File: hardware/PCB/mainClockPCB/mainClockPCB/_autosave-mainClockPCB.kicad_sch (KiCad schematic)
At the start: 51 parts, among them IC2 SPX1117M3-L_TR, IC3 MCP7940N-I_P, IC4 PAM8904QJER, J1 USB_C_Receptacle_USB2.0_16P, J2 Conn_01x09_Socket, J3 Conn_01x02_Socket, J4 Conn_01x09_Socket, J5 Conn_01x06, SW1 SW_Push, SW2 SW_Push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

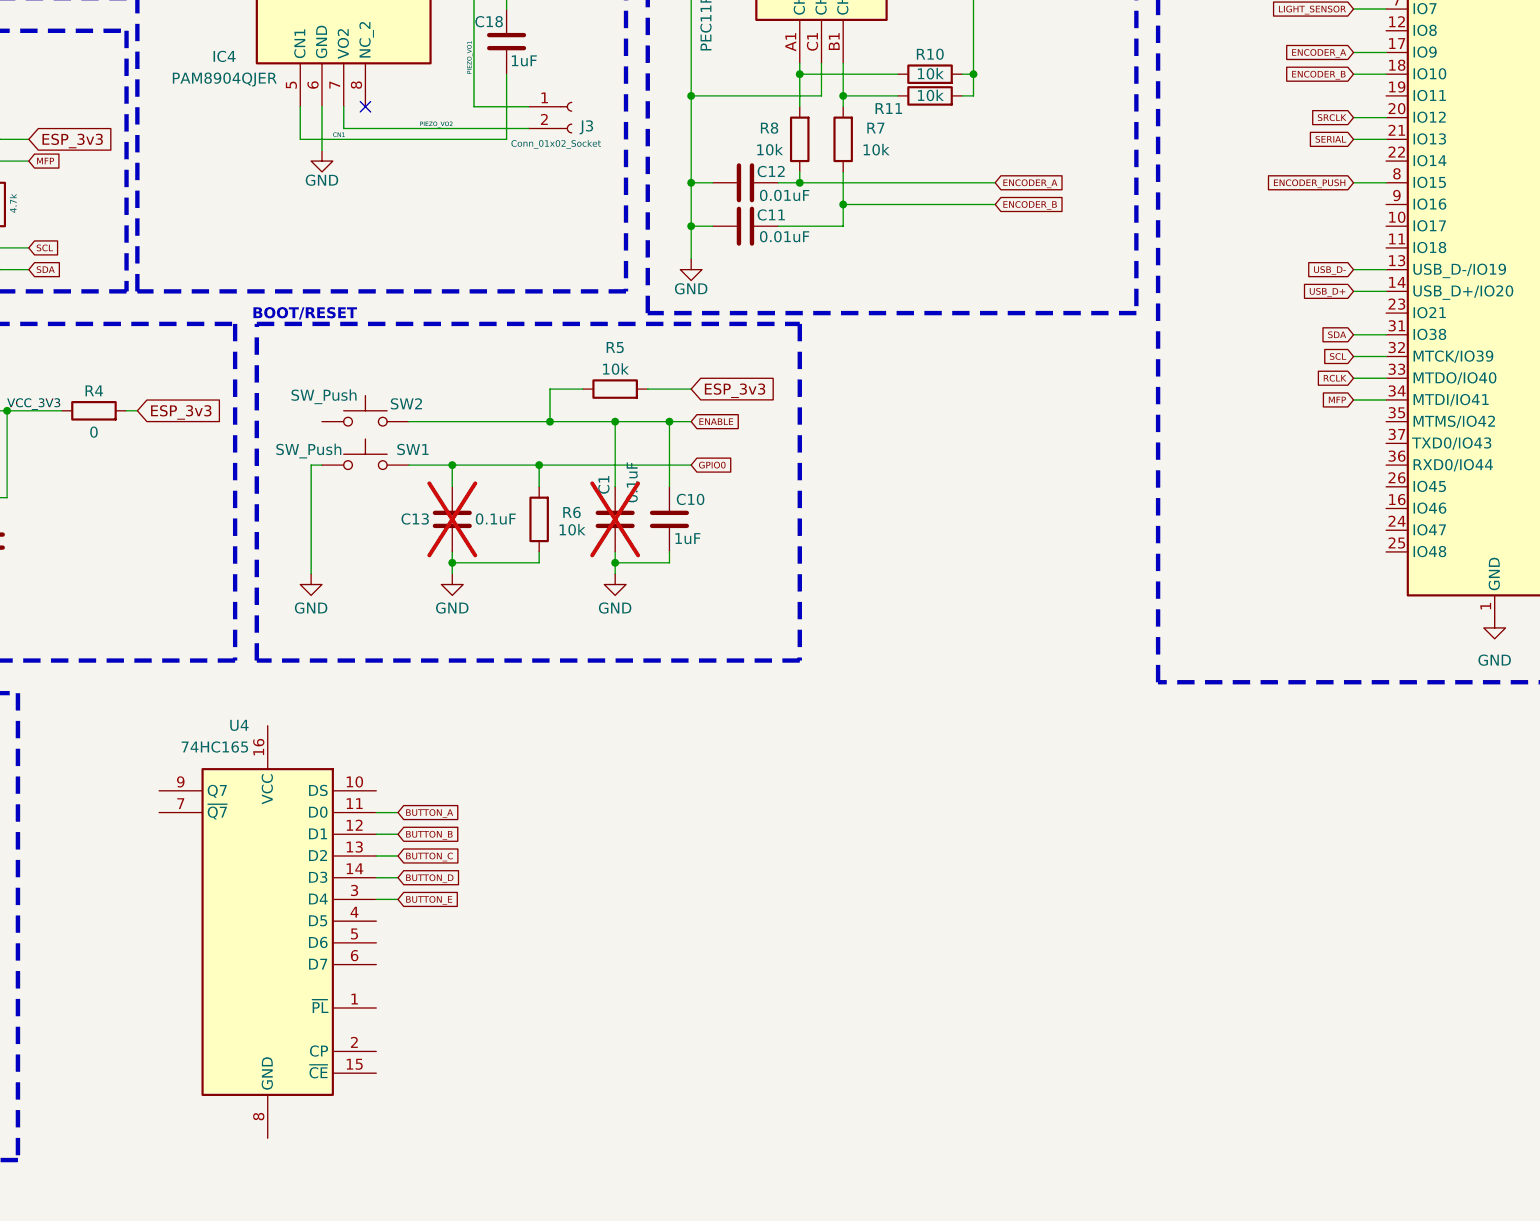
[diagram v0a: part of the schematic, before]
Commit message: button header amd PISO register
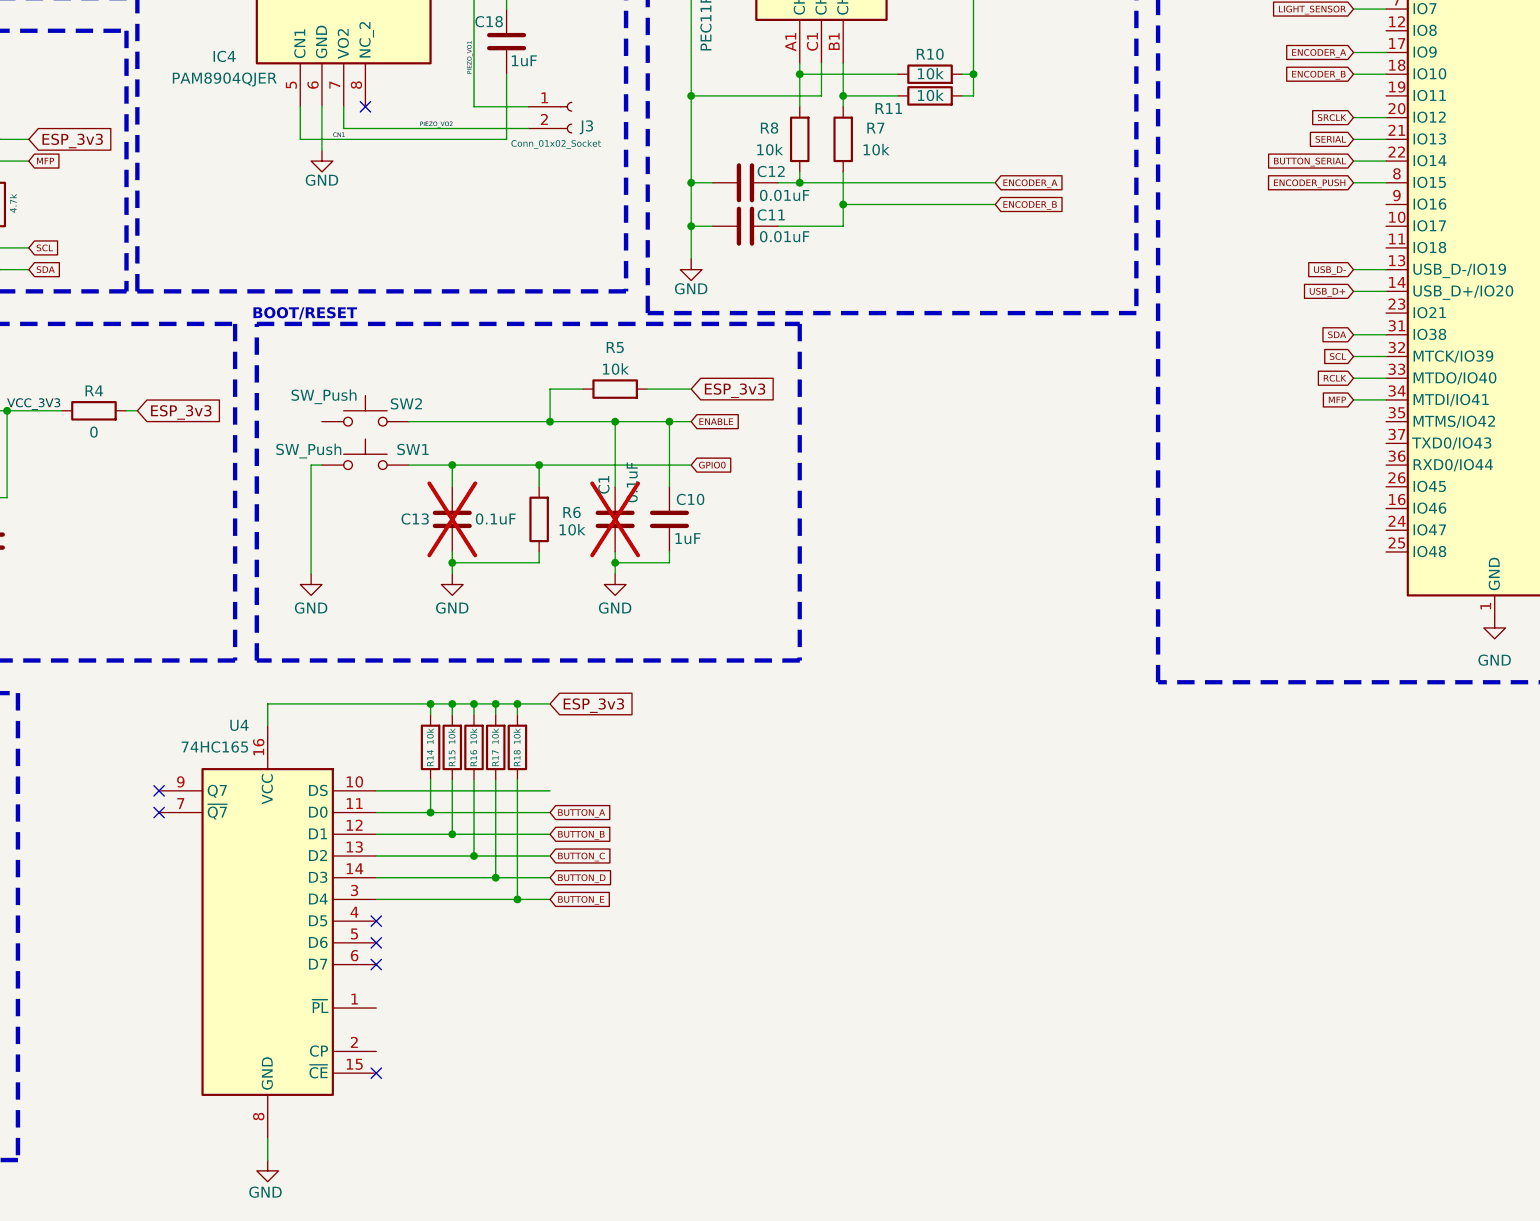
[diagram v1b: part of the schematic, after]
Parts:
- added R14, R15, R16, R17, R18: 10k, Resistor_SMD:R_0603_1608Metric_Pad0.98x0.95mm_HandSolder, symbol Device:R
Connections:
- net BUTTON_A: now also R14.1
- net BUTTON_B: now also R15.1
- net BUTTON_C: now also R16.1
- net BUTTON_D: now also R17.1
- net BUTTON_E: now also R18.1
- net ESP_3v3: now also U4.16 (VCC), R14.2, R15.2, R16.2, R17.2, R18.2
- net GND: now also U4.8 (GND)
- net BUTTON_SERIAL: now reaches U3.22 (IO14)
- no-connect marks 6 -> 12
